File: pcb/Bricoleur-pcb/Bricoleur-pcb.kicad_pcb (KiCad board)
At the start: 2 copper layers, 54 parts, among them J1 USB_B_Micro, J2 Conn_02x10_Odd_Even, SW2 SW_Push, SW3 SW_Push, SW4 SW_Push, SW5 SW_Push, U1 Ultrasonic-LV-EZ0, U10 VESD05A8A-HNH, U11 SW_DP3T, U2 PYNQ-Shield-Bricoleur-pcb-cac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, U3 Ultrasonic-LV-EZ0, U4 Ultrasonic-LV-EZ0, U5 Arducam-OV5642, U6 Arducam-OV5642, U7 EFM32GG980, U8 UART_BOOT

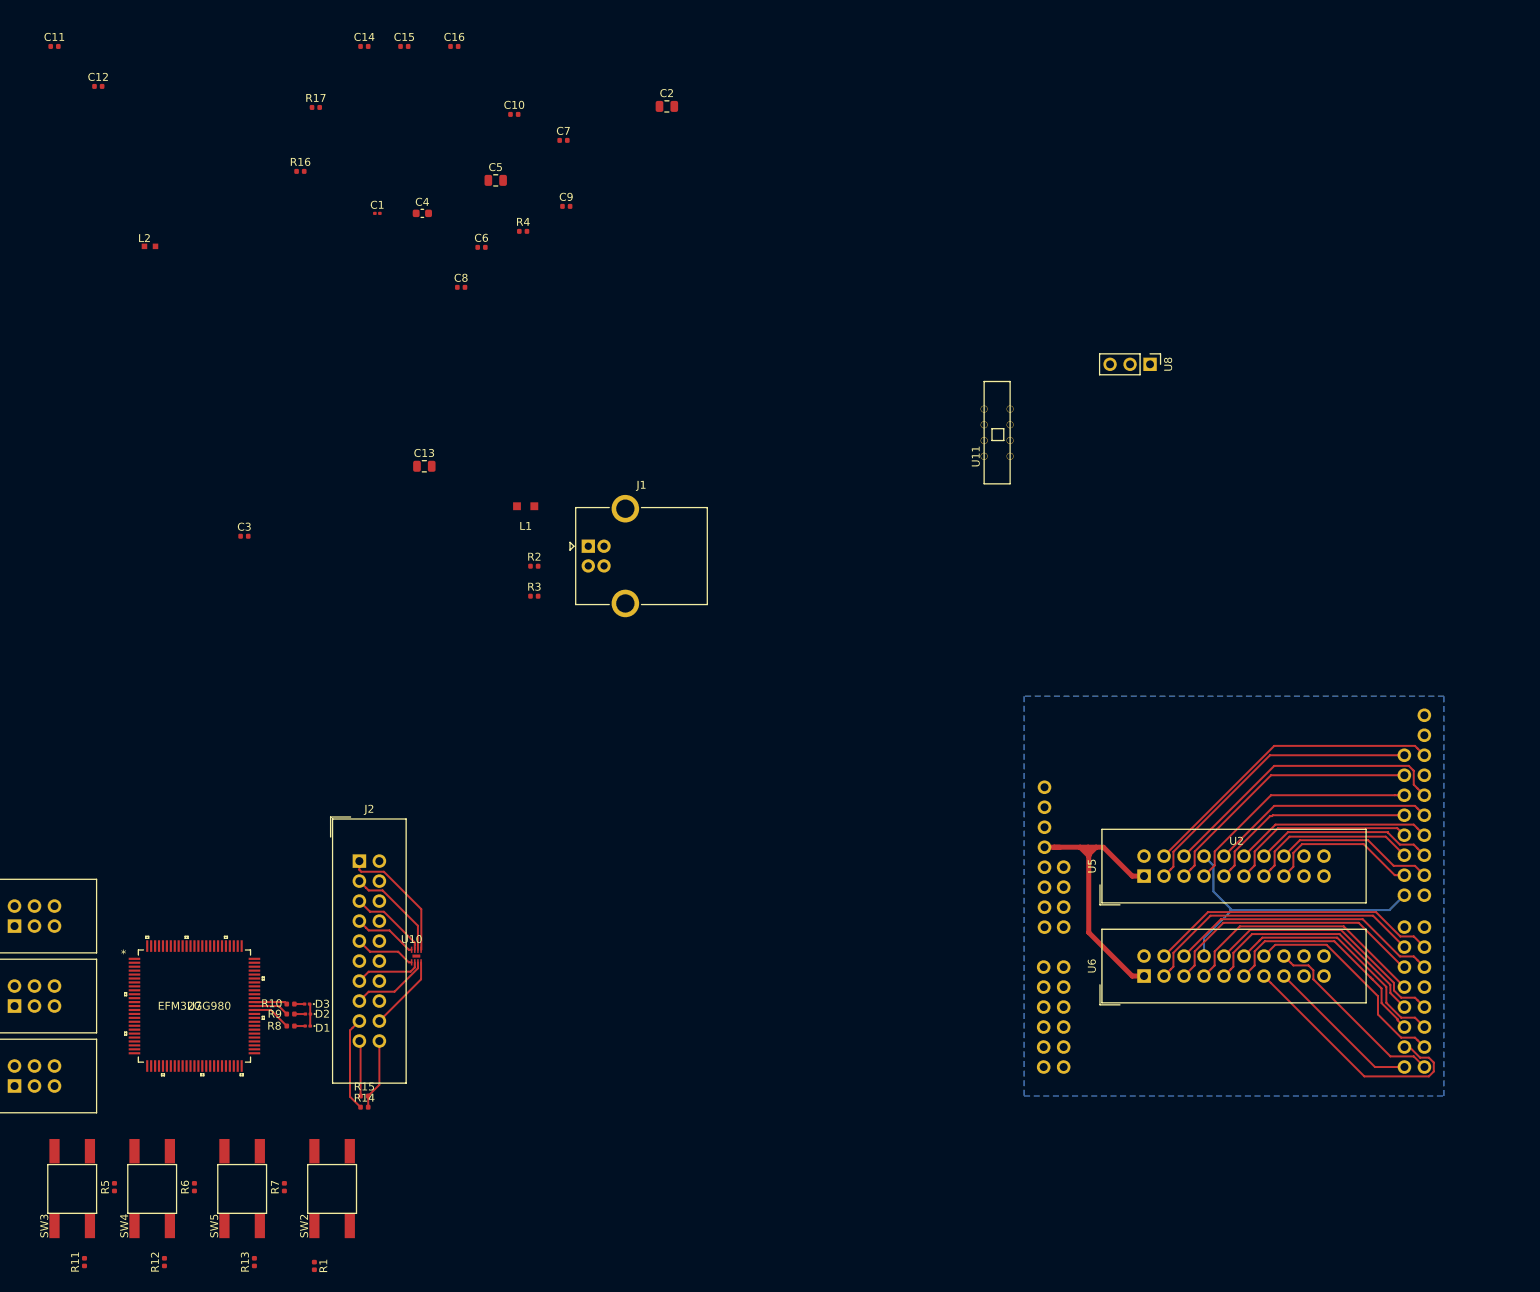
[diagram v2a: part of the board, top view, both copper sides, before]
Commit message: More ESD protection, USART output, more footprints
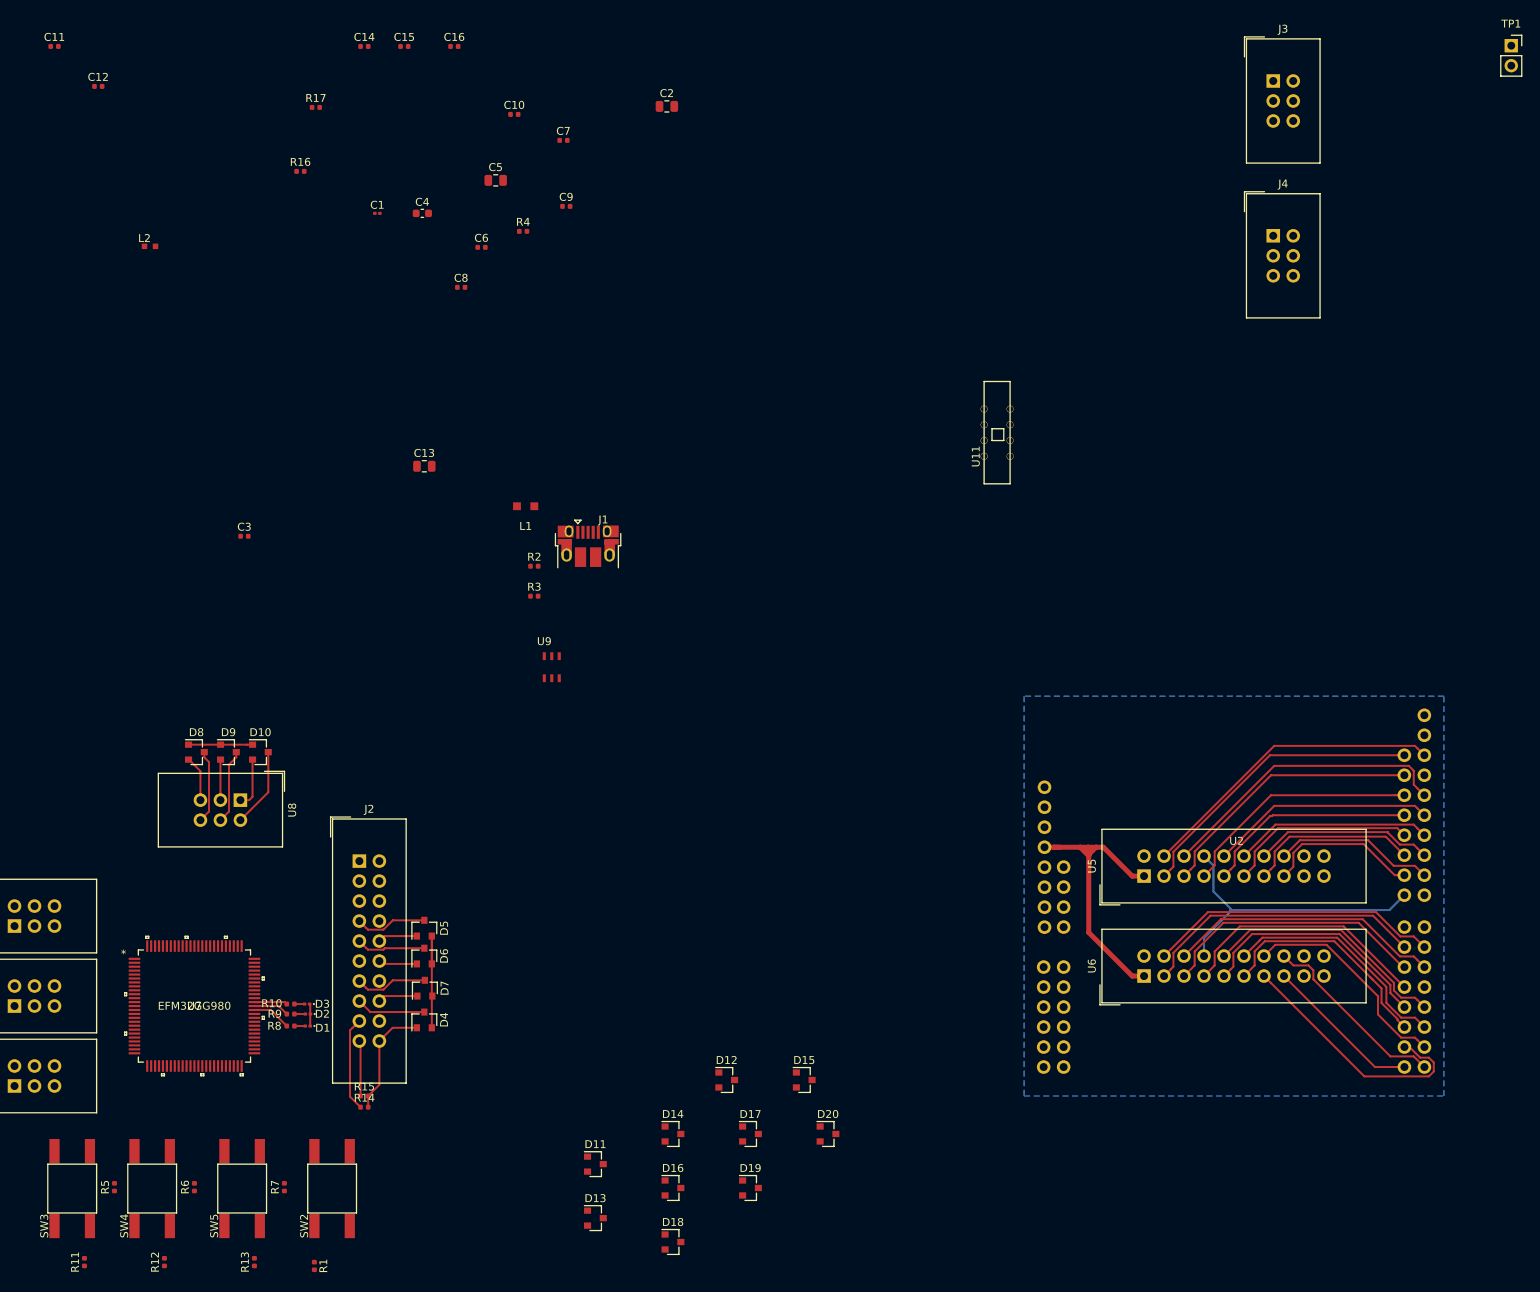
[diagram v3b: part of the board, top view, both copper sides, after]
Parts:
- removed U10: VESD05A8A-HNH, Bricoleur-custom:VESD05A8A-HNH
- added D10: BAT54S, Package_TO_SOT_SMD:SOT-23, F.Cu at (124.0, 111.3)
- added D11: BAT54S, Package_TO_SOT_SMD:SOT-23, F.Cu at (166.5, 163.6)
- added D12: BAT54S, Package_TO_SOT_SMD:SOT-23, F.Cu at (183.2, 152.9)
- added D13: BAT54S, Package_TO_SOT_SMD:SOT-23, F.Cu at (166.5, 170.5)
- added D14: BAT54S, Package_TO_SOT_SMD:SOT-23, F.Cu at (176.4, 159.8)
- added D15: BAT54S, Package_TO_SOT_SMD:SOT-23, F.Cu at (193.0, 152.9)
- added D16: BAT54S, Package_TO_SOT_SMD:SOT-23, F.Cu at (176.4, 166.6)
- added D17: BAT54S, Package_TO_SOT_SMD:SOT-23, F.Cu at (186.2, 159.8)
- added D18: BAT54S, Package_TO_SOT_SMD:SOT-23, F.Cu at (176.4, 173.5)
- added D19: BAT54S, Package_TO_SOT_SMD:SOT-23, F.Cu at (186.2, 166.6)
- added D20: BAT54S, Package_TO_SOT_SMD:SOT-23, F.Cu at (196.1, 159.8)
- added D4: BAT54S, Package_TO_SOT_SMD:SOT-23, F.Cu at (144.8, 145.3)
- added D5: BAT54S, Package_TO_SOT_SMD:SOT-23, F.Cu at (144.8, 133.6)
- added D6: BAT54S, Package_TO_SOT_SMD:SOT-23, F.Cu at (144.8, 137.2)
- added D7: BAT54S, Package_TO_SOT_SMD:SOT-23, F.Cu at (144.8, 141.2)
- added D8: BAT54S, Package_TO_SOT_SMD:SOT-23, F.Cu at (115.8, 111.3)
- added D9: BAT54S, Package_TO_SOT_SMD:SOT-23, F.Cu at (119.9, 111.3)
- added J3: Conn_02x03_Odd_Even, Connector_IDC:IDC-Header_2x03_P2.54mm_Vertical, F.Cu at (252.6, 26.0)
- added J4: Conn_02x03_Odd_Even, Connector_IDC:IDC-Header_2x03_P2.54mm_Vertical, F.Cu at (252.6, 45.7)
- added TP1: Test_VMCU, Connector_PinSocket_2.54mm:PinSocket_1x02_P2.54mm_Vertical, F.Cu at (282.9, 21.5)
- added U9: IP4220CZ6, Bricoleur-custom:IP4220CZ6, F.Cu at (160.0, 99.1)
- J1: footprint Connector_USB:USB_B_OST_USB-B1HSxx_Horizontal -> Connector_USB:USB_Micro-B_Amphenol_10103594-0001LF_Horizontal
- U8: footprint Connector_PinHeader_2.54mm:PinHeader_1x03_P2.54mm_Vertical -> Connector_IDC:IDC-Header_2x03_P2.54mm_Vertical
- moved U8 128.2 mm to (121.4, 117.3)
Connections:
- J1 pad 4: (no net) -> Net-(J1-Pad4)
- J2 pad 2: (no net) -> Net-(J2-Pad2)
- J2 pad 3: DH_#TRST -> Net-(J2-Pad3)
- J2 pad 5: DH_TDI -> Net-(J2-Pad5)
- U1 pad 1: (no net) -> PULSE
- U1 pad 2: PULSE -> Net-(U1-Pad2)
- U1 pad 3: (no net) -> /Ultra/RX0
- U1 pad 5: (no net) -> /Ultra/PYNQ_3V3
- U1 pad 6: PYNQ_3V3 -> /Ultra/GND
- U11 pad 4: (no net) -> Net-(U11-Pad4)
- U2 pad 1: (no net) -> Net-(U2-Pad1)
- U2 pad 10: (no net) -> Net-(U2-Pad10)
- U2 pad 11: (no net) -> Net-(U2-Pad11)
- U2 pad 12: (no net) -> Net-(U2-Pad12)
- U2 pad 13: (no net) -> Net-(U2-Pad13)
- U2 pad 14: (no net) -> Net-(U2-Pad14)
- U2 pad 15: (no net) -> Net-(U2-Pad15)
- U2 pad 16: (no net) -> Net-(U2-Pad16)
- U2 pad 17: (no net) -> Net-(U2-Pad17)
- U2 pad 18: (no net) -> Net-(U2-Pad18)
- U2 pad 19: (no net) -> Net-(U2-Pad19)
- U2 pad 2: (no net) -> Net-(U2-Pad2)
- U2 pad 20: (no net) -> Net-(U2-Pad20)
- U2 pad 21: (no net) -> Net-(U2-Pad21)
- U2 pad 22: (no net) -> Net-(U2-Pad22)
- U2 pad 23: (no net) -> Net-(U2-Pad23)
- U2 pad 24: (no net) -> Net-(U2-Pad24)
- U2 pad 25: (no net) -> Net-(U2-Pad25)
- U2 pad 26: (no net) -> Net-(U2-Pad26)
- U2 pad 28: (no net) -> Net-(U2-Pad28)
- U2 pad 3: (no net) -> Net-(U2-Pad3)
- U2 pad 34: /US0_CS -> Net-(U2-Pad34)
- U2 pad 5: (no net) -> /PYNQ_5V0
- U2 pad 8: (no net) -> Net-(U2-Pad8)
- U2 pad 9: (no net) -> Net-(U2-Pad9)
- U3 pad 1: (no net) -> PULSE
- U3 pad 2: PULSE -> Net-(U3-Pad2)
- U3 pad 3: (no net) -> /Ultra/RX1
- U3 pad 5: (no net) -> /Ultra/PYNQ_3V3
- U3 pad 6: PYNQ_3V3 -> /Ultra/GND
- U4 pad 1: (no net) -> PULSE
- U4 pad 2: PULSE -> Net-(U4-Pad2)
- U4 pad 3: (no net) -> /Ultra/RX2
- U4 pad 5: (no net) -> /Ultra/PYNQ_3V3
- U4 pad 6: PYNQ_3V3 -> /Ultra/GND
- U5 pad 18: (no net) -> Net-(U5-Pad18)
- U5 pad 19: (no net) -> Net-(U5-Pad19)
- U5 pad 20: (no net) -> Net-(U5-Pad20)
- U6 pad 18: (no net) -> Net-(U6-Pad18)
- U6 pad 19: (no net) -> Net-(U6-Pad19)
- U6 pad 20: (no net) -> Net-(U6-Pad20)
- U7 pad 100: (no net) -> Net-(U7-Pad100)
- U7 pad 11: (no net) -> Net-(U7-Pad11)
- U7 pad 12: (no net) -> Net-(U7-Pad12)
- U7 pad 13: (no net) -> Net-(U7-Pad13)
- U7 pad 14: (no net) -> Net-(U7-Pad14)
- U7 pad 15: (no net) -> Net-(U7-Pad15)
- U7 pad 18: (no net) -> /US1_TX
- U7 pad 19: (no net) -> /US1_RX
- U7 pad 2: (no net) -> Net-(U7-Pad2)
- U7 pad 20: (no net) -> Net-(U7-Pad20)
- U7 pad 21: (no net) -> Net-(U7-Pad21)
- U7 pad 22: (no net) -> Net-(U7-Pad22)
- U7 pad 23: (no net) -> Net-(U7-Pad23)
- U7 pad 24: (no net) -> /US1_CLK
- U7 pad 25: (no net) -> Net-(U7-Pad25)
- U7 pad 26: (no net) -> Net-(U7-Pad26)
- U7 pad 27: (no net) -> Net-(U7-Pad27)
- U7 pad 28: (no net) -> Net-(U7-Pad28)
- U7 pad 29: (no net) -> Net-(U7-Pad29)
- U7 pad 3: (no net) -> Net-(U7-Pad3)
- U7 pad 30: (no net) -> Net-(U7-Pad30)
- U7 pad 32: (no net) -> /VSS07
- U7 pad 33: (no net) -> Net-(U7-Pad33)
- U7 pad 34: (no net) -> Net-(U7-Pad34)
- U7 pad 35: (no net) -> Net-(U7-Pad35)
- U7 pad 4: Net-(U1-Pad4) -> /Ultra/RX0
- U7 pad 40: (no net) -> Net-(U7-Pad40)
- U7 pad 42: (no net) -> Net-(U7-Pad42)
- U7 pad 43: (no net) -> Net-(U7-Pad43)
- U7 pad 46: (no net) -> Net-(U7-Pad46)
- U7 pad 47: (no net) -> Net-(U7-Pad47)
- U7 pad 48: (no net) -> Net-(U7-Pad48)
- U7 pad 49: (no net) -> Net-(U7-Pad49)
- U7 pad 5: Net-(U4-Pad4) -> /Ultra/RX1
- U7 pad 50: (no net) -> Net-(U7-Pad50)
- U7 pad 51: (no net) -> Net-(U7-Pad51)
- U7 pad 52: (no net) -> Net-(U7-Pad52)
- U7 pad 53: (no net) -> Net-(U7-Pad53)
- U7 pad 54: (no net) -> Net-(U7-Pad54)
- U7 pad 55: (no net) -> Net-(U7-Pad55)
- U7 pad 56: (no net) -> Net-(U7-Pad56)
- U7 pad 6: Net-(U3-Pad4) -> /Ultra/RX2
- U7 pad 60: (no net) -> Net-(U7-Pad60)
- U7 pad 61: (no net) -> Net-(U7-Pad61)
- U7 pad 65: (no net) -> Net-(U7-Pad65)
- U7 pad 66: (no net) -> Net-(U7-Pad66)
- U7 pad 67: (no net) -> Net-(U7-Pad67)
- U7 pad 68: /US0_CS -> Net-(U7-Pad68)
- U7 pad 7: (no net) -> Net-(U7-Pad7)
- U7 pad 80: (no net) -> Net-(U7-Pad80)
- U7 pad 81: (no net) -> Net-(U7-Pad81)
- U7 pad 84: (no net) -> Net-(U7-Pad84)
- U7 pad 85: (no net) -> Net-(U7-Pad85)
- U7 pad 86: (no net) -> Net-(U7-Pad86)
- U7 pad 87: (no net) -> Net-(U7-Pad87)
- U7 pad 88: (no net) -> Net-(U7-Pad88)
- U7 pad 89: (no net) -> Net-(U7-Pad89)
- U7 pad 9: (no net) -> Net-(U7-Pad9)
- U7 pad 90: (no net) -> Net-(U7-Pad90)
- U7 pad 91: (no net) -> Net-(U7-Pad91)
- U7 pad 92: (no net) -> Net-(U7-Pad92)
- U7 pad 93: (no net) -> Net-(U7-Pad93)
- U7 pad 94: Net-(U7-Pad94) -> /sheet5BB7B6EA/INP
- U7 pad 95: Net-(U7-Pad95) -> /Sheet5BB71F0E/INP
- U7 pad 96: (no net) -> Net-(U7-Pad96)
- U7 pad 97: (no net) -> Net-(U7-Pad97)
- U7 pad 98: (no net) -> Net-(U7-Pad98)
- U7 pad 99: (no net) -> Net-(U7-Pad99)
- U8 pad 1: Net-(U7-Pad94) -> GND
- U8 pad 2: Net-(U7-Pad95) -> DH_TCK_SWCLK
- U8 pad 3: DH_TCK_SWCLK -> GND
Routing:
- net GND: track 11.8 -> 49.7 mm
- net DH_#TRST: track 12.8 -> 0.00 mm
- net DH_TCK_SWCLK: track 7.76 -> 18.9 mm
- net DH_TDI: track 10.1 -> 0.00 mm
- net DEBUG_EXT_CABLE_ATTACH: track 9.65 -> 0.00 mm
- net /sheet5BB7B6EA/INP: track 0.00 -> 9.47 mm
- net /Sheet5BB71F0E/INP: track 0.00 -> 9.34 mm
- net DH_VTARGET: track 16.2 -> 23.3 mm
- net DH_#RESET: track 9.92 -> 8.83 mm
- net DH_TMS_SWDIO: track 8.15 -> 9.20 mm
- net DH_TDO_SWO: track 8.41 -> 9.26 mm

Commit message: PCB…
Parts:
- moved J4 242.4 mm to (51.3, 180.6), turned to 180 degrees
- moved U2 201.6 mm to (52.3, 78.6), turned to 0 degrees
- moved U6 188.0 mm to (65.0, 62.2), turned to 270 degrees
- moved J3 182.0 mm to (160.7, 183.1), turned to 90 degrees
- moved U5 179.0 mm to (65.0, 74.9), turned to 270 degrees
- moved D14 156.9 mm to (22.3, 130.1), turned to 180 degrees
- moved D12 154.3 mm to (36.7, 104.6), turned to 180 degrees
- moved D20 153.8 mm to (43.2, 177.5), turned to 90 degrees
- moved D19 143.1 mm to (43.2, 173.3), turned to 90 degrees
- moved D11 139.0 mm to (36.7, 113.9), turned to 180 degrees
- moved D13 138.2 mm to (36.7, 123.2), turned to 180 degrees
- moved D18 133.4 mm to (43.2, 181.6), turned to 90 degrees
- moved J1 102.7 mm to (200.5, 181.7)
- moved L1 100.6 mm to (212.4, 164.4)
- moved R2 93.8 mm to (68.1, 111.4), turned to 270 degrees
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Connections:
- C10 pad 1: DH_VTARGET -> VMCU
- C11 pad 1: DH_VTARGET -> VMCU
- C12 pad 1: DH_VTARGET -> VMCU
- C13 pad 1: DH_VTARGET -> VMCU
- C8 pad 1: DH_VTARGET -> VMCU
- C9 pad 1: DH_VTARGET -> VMCU
- D10 pad 1: DH_VTARGET -> VMCU
- D11 pad 1: DH_VTARGET -> VMCU
- D12 pad 1: DH_VTARGET -> VMCU
- D13 pad 1: DH_VTARGET -> VMCU
- D14 pad 1: DH_VTARGET -> VMCU
- D15 pad 1: DH_VTARGET -> VMCU
- D16 pad 1: DH_VTARGET -> VMCU
- D17 pad 1: DH_VTARGET -> VMCU
- D18 pad 1: DH_VTARGET -> VMCU
- D19 pad 1: DH_VTARGET -> VMCU
- D20 pad 1: DH_VTARGET -> VMCU
- D4 pad 2: DH_VTARGET -> VMCU
- D5 pad 2: DH_VTARGET -> VMCU
- D6 pad 2: DH_VTARGET -> VMCU
- D7 pad 2: DH_VTARGET -> VMCU
- D8 pad 1: DH_VTARGET -> VMCU
- D9 pad 1: DH_VTARGET -> VMCU
- J1 pad 4: Net-(J1-Pad4) -> (no net)
- J2 pad 1: DH_VTARGET -> VMCU
- J2 pad 2: Net-(J2-Pad2) -> (no net)
- J2 pad 3: Net-(J2-Pad3) -> (no net)
- J2 pad 5: Net-(J2-Pad5) -> (no net)
- L2 pad 1: DH_VTARGET -> VMCU
- R5 pad 2: DH_VTARGET -> VMCU
- R6 pad 2: DH_VTARGET -> VMCU
- R7 pad 2: DH_VTARGET -> VMCU
- TP1 pad 1: DH_VTARGET -> VMCU
- U1 pad 2: Net-(U1-Pad2) -> (no net)
- U1 pad 4: Net-(U1-Pad4) -> (no net)
- U1 pad 5: /Ultra/PYNQ_3V3 -> VMCU
- U1 pad 6: /Ultra/GND -> GND
- U11 pad 1: DH_VTARGET -> VMCU
- U2 pad 1: Net-(U2-Pad1) -> (no net)
- U2 pad 10: Net-(U2-Pad10) -> (no net)
- U2 pad 11: Net-(U2-Pad11) -> (no net)
- U2 pad 12: Net-(U2-Pad12) -> (no net)
- U2 pad 13: Net-(U2-Pad13) -> (no net)
- U2 pad 14: Net-(U2-Pad14) -> (no net)
- U2 pad 15: Net-(U2-Pad15) -> (no net)
- U2 pad 16: Net-(U2-Pad16) -> (no net)
- U2 pad 17: Net-(U2-Pad17) -> (no net)
- U2 pad 18: Net-(U2-Pad18) -> (no net)
- U2 pad 19: Net-(U2-Pad19) -> (no net)
- U2 pad 2: Net-(U2-Pad2) -> (no net)
- U2 pad 20: Net-(U2-Pad20) -> (no net)
- U2 pad 21: Net-(U2-Pad21) -> (no net)
- U2 pad 22: Net-(U2-Pad22) -> (no net)
- U2 pad 23: Net-(U2-Pad23) -> (no net)
- U2 pad 24: Net-(U2-Pad24) -> (no net)
- U2 pad 25: Net-(U2-Pad25) -> (no net)
- U2 pad 26: Net-(U2-Pad26) -> (no net)
- U2 pad 28: Net-(U2-Pad28) -> (no net)
- U2 pad 3: Net-(U2-Pad3) -> (no net)
- U2 pad 34: Net-(U2-Pad34) -> (no net)
- U2 pad 5: /PYNQ_5V0 -> (no net)
- U2 pad 8: Net-(U2-Pad8) -> (no net)
- U2 pad 9: Net-(U2-Pad9) -> (no net)
- U3 pad 2: Net-(U3-Pad2) -> (no net)
- U3 pad 4: Net-(U3-Pad4) -> (no net)
- U3 pad 5: /Ultra/PYNQ_3V3 -> VMCU
- U3 pad 6: /Ultra/GND -> GND
- U4 pad 2: Net-(U4-Pad2) -> (no net)
- U4 pad 4: Net-(U4-Pad4) -> (no net)
- U4 pad 5: /Ultra/PYNQ_3V3 -> VMCU
- U4 pad 6: /Ultra/GND -> GND
- U5 pad 18: Net-(U5-Pad18) -> (no net)
- U5 pad 19: Net-(U5-Pad19) -> (no net)
- U5 pad 20: Net-(U5-Pad20) -> (no net)
- U6 pad 18: Net-(U6-Pad18) -> (no net)
- U6 pad 19: Net-(U6-Pad19) -> (no net)
- U6 pad 20: Net-(U6-Pad20) -> (no net)
- U7 pad 100: Net-(U7-Pad100) -> (no net)
- U7 pad 11: Net-(U7-Pad11) -> (no net)
- U7 pad 12: Net-(U7-Pad12) -> (no net)
- U7 pad 13: Net-(U7-Pad13) -> (no net)
- U7 pad 14: Net-(U7-Pad14) -> (no net)
- U7 pad 15: Net-(U7-Pad15) -> (no net)
- U7 pad 17: DH_VTARGET -> VMCU
- U7 pad 2: Net-(U7-Pad2) -> (no net)
- U7 pad 20: Net-(U7-Pad20) -> (no net)
- U7 pad 21: Net-(U7-Pad21) -> (no net)
- U7 pad 22: Net-(U7-Pad22) -> (no net)
- U7 pad 23: Net-(U7-Pad23) -> (no net)
- U7 pad 25: Net-(U7-Pad25) -> (no net)
- U7 pad 26: Net-(U7-Pad26) -> (no net)
- U7 pad 27: Net-(U7-Pad27) -> (no net)
- U7 pad 28: Net-(U7-Pad28) -> (no net)
- U7 pad 29: Net-(U7-Pad29) -> (no net)
- U7 pad 3: Net-(U7-Pad3) -> (no net)
- U7 pad 30: Net-(U7-Pad30) -> (no net)
- U7 pad 31: DH_VTARGET -> VMCU
- U7 pad 32: /VSS07 -> (no net)
- U7 pad 33: Net-(U7-Pad33) -> (no net)
- U7 pad 34: Net-(U7-Pad34) -> (no net)
- U7 pad 35: Net-(U7-Pad35) -> (no net)
- U7 pad 40: Net-(U7-Pad40) -> (no net)
- U7 pad 42: Net-(U7-Pad42) -> (no net)
- U7 pad 43: Net-(U7-Pad43) -> (no net)
- U7 pad 44: DH_VTARGET -> VMCU
- U7 pad 46: Net-(U7-Pad46) -> (no net)
- U7 pad 47: Net-(U7-Pad47) -> (no net)
- U7 pad 48: Net-(U7-Pad48) -> (no net)
- U7 pad 49: Net-(U7-Pad49) -> (no net)
- U7 pad 50: Net-(U7-Pad50) -> (no net)
- U7 pad 51: Net-(U7-Pad51) -> (no net)
- U7 pad 52: Net-(U7-Pad52) -> (no net)
- U7 pad 53: Net-(U7-Pad53) -> (no net)
- U7 pad 54: Net-(U7-Pad54) -> (no net)
- U7 pad 55: Net-(U7-Pad55) -> (no net)
- U7 pad 56: Net-(U7-Pad56) -> (no net)
- U7 pad 57: DH_VTARGET -> VMCU
- U7 pad 60: Net-(U7-Pad60) -> (no net)
- U7 pad 61: Net-(U7-Pad61) -> (no net)
- U7 pad 65: Net-(U7-Pad65) -> (no net)
- U7 pad 66: Net-(U7-Pad66) -> (no net)
- U7 pad 67: Net-(U7-Pad67) -> (no net)
- U7 pad 68: Net-(U7-Pad68) -> (no net)
- U7 pad 7: Net-(U7-Pad7) -> (no net)
- U7 pad 8: DH_VTARGET -> VMCU
- U7 pad 80: Net-(U7-Pad80) -> (no net)
- U7 pad 81: Net-(U7-Pad81) -> (no net)
- U7 pad 82: DH_VTARGET -> VMCU
- U7 pad 84: Net-(U7-Pad84) -> (no net)
- U7 pad 85: Net-(U7-Pad85) -> (no net)
- U7 pad 86: Net-(U7-Pad86) -> (no net)
- U7 pad 87: Net-(U7-Pad87) -> (no net)
- U7 pad 88: Net-(U7-Pad88) -> (no net)
- U7 pad 89: Net-(U7-Pad89) -> (no net)
- U7 pad 9: Net-(U7-Pad9) -> (no net)
- U7 pad 90: Net-(U7-Pad90) -> (no net)
- U7 pad 91: Net-(U7-Pad91) -> (no net)
- U7 pad 92: Net-(U7-Pad92) -> (no net)
- U7 pad 93: Net-(U7-Pad93) -> (no net)
- U7 pad 96: Net-(U7-Pad96) -> (no net)
- U7 pad 97: Net-(U7-Pad97) -> (no net)
- U7 pad 98: Net-(U7-Pad98) -> (no net)
- U7 pad 99: Net-(U7-Pad99) -> (no net)
- U9 pad 1: Net-(U9-Pad1) -> (no net)
- U9 pad 3: Net-(U9-Pad3) -> (no net)
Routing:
- net GND: track 49.7 -> 157.4 mm
- net VMCU: track 0.00 -> 102.3 mm
- net PULSE: track 0.00 -> 30.4 mm
- net DH_VTARGET: track 23.3 -> 0.00 mm
- net DBG_PB_1: track 0.00 -> 13.5 mm
- net DBG_PB_2: track 0.00 -> 13.4 mm
- net DBG_PB_3: track 0.00 -> 13.4 mm
- net Net-(R12-Pad2): track 0.00 -> 13.4 mm
- net Net-(R13-Pad2): track 0.00 -> 13.4 mm
- net Net-(R11-Pad2): track 0.00 -> 13.2 mm
- net Net-(R1-Pad1): track 0.00 -> 12.2 mm
- net /Ultra/RX1: track 0.00 -> 10.2 mm
- net /Ultra/RX0: track 0.00 -> 10.2 mm
- net /Ultra/RX2: track 0.00 -> 10.1 mm
- net /US1_CLK: track 0.00 -> 9.91 mm
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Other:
- net class Power: trace_width 0.254 -> 0.635
